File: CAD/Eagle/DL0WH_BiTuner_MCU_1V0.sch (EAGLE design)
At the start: 133 parts, among them Q0321 ABS07-32.768KHZ, U0101 STM32L476RXT_64PIN_LDO, U2401 LM53603-Q1, U8921 TS5A23166, U8951 OPA354, U9001 TPS62051, U9401 MC33996, U9501 MC33996, U9601 MC33996, U9801 MAX232_SOIC16, U9901 MAX232_SOIC16, X2411 WIRE-TO-BOARD_5MM08_1X02, X3201 MOLEX 105017-0001, X3301 SMA_SMT_AMPHENOL-901-143, X3311 SAMTEC SMA-J-P-H-RA-TH1, X9851 WIRE-TO-BOARD_5MM08_1X02, X9852 WIRE-TO-BOARD_5MM08_1X02, X9853 WIRE-TO-BOARD_5MM08_1X02, X9951 WIRE-TO-BOARD_5MM08_1X02, X9952 WIRE-TO-BOARD_5MM08_1X02, X9953 WIRE-TO-BOARD_5MM08_1X02

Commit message: HW_1V0 - CAD/Eagle - some routing done
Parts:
- L9011: device df4iah_rcl:L-EUL0603 -> df4iah_rcl:L-EU8.00X8.00MM
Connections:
- removed net +5V0: C2421.1, C2422.1, C2423.1, C9001.1, L2411.1, R2411.2, R9002.2, U2401.FB, U9001.EN, U9001.VIN
- removed net DC_12V_IN: C2401.1, C2402.1, C2403.1, C2404.1, U2401.EN, U2401.VIN@12, U2401.VIN@13, X2411.1
- net +12V: now also C2401.1, C2402.1, C2403.1, C2404.1, U2401.EN, U2401.VIN@12, U2401.VIN@13, X2411.1
- net +5V: now also C2421.1, C2422.1, C2423.1, C9001.1, L2411.1, R2411.2, R9002.2, U2401.FB, U9001.EN, U9001.VIN
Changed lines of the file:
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@@
 <part name="R9424" library="df4iah_rcl" deviceset="R-EU_" device="R0603" value="47R"/>
 <part name="U9001" library="df4iah_powersupply" deviceset="TPS62051" device=""/>
-<part name="L9011" library="df4iah_rcl" deviceset="L-EU" device="L0603" value="10uH"/>
+<part name="L9011" library="df4iah_rcl" deviceset="L-EU" device="8.00X8.00MM" value="10uH"/>
 <part name="R9021" library="df4iah_rcl" deviceset="R-EU_" device="R0603" value="1MR"/>
 <part name="R9022" library="df4iah_rcl" deviceset="R-EU_" device="R0603" value="1MR"/>
@@
 </busses>
 <nets>
-<net name="+5V0" class="0">
+<net name="+5V" class="2">
 <segment>
 <wire x1="182.88" y1="124.46" x2="195.58" y2="124.46" width="0.1524" layer="91"/>
@@
 </segment>
 </net>
-<net name="DC_12V_IN" class="0">
+<net name="+12V" class="0">
 <segment>
 <label x="22.86" y="124.46" size="1.778" layer="95" rot="R180" xref="yes"/>
@@
 </segment>
 </net>
-<net name="+5V0" class="0">
+<net name="+5V" class="2">
 <segment>
 <pinref part="U9001" gate="G$1" pin="VIN"/>

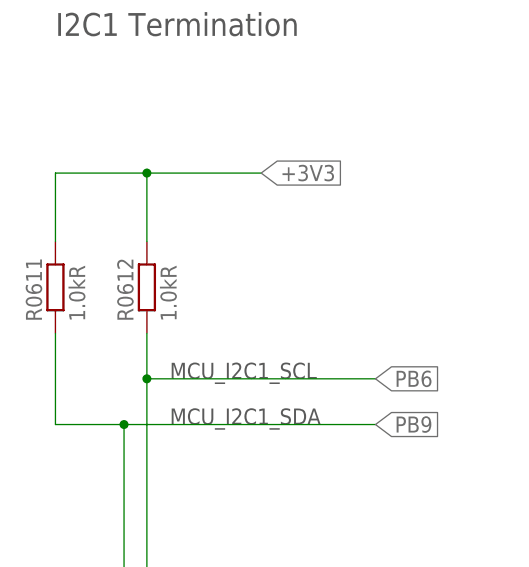
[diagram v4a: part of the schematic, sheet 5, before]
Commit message: HW_1V0 - CAD/Eagle - prepared BOM and adjusted some package sizes - still L9011 needs correct package
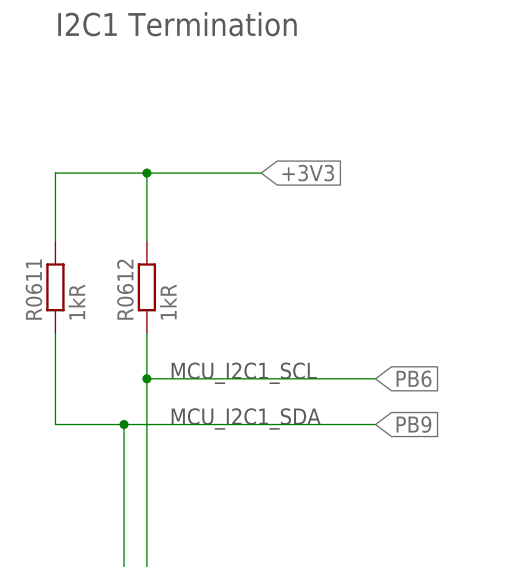
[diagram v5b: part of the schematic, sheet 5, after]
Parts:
- C0410, C2401, C2402, C2403, C2405, C2421, C2422, C2423: device df4iah_rcl:C-EUC0402 -> df4iah_rcl:C-EUC0603
- C8901, C8911, C8921, C8951, C9401, C9402, C9501, C9502, C9601, C9602: device df4iah_rcl:C-EUC0603 -> df4iah_rcl:C-EUC0402
- C9001, C9011: device df4iah_rcl:C-EUC0805 -> df4iah_rcl:C-EUC0603
- C9801, C9802, C9803, C9804, C9805, C9901, C9902, C9903, C9904, C9905: device rcl:C-EUC0805 -> df4iah_rcl:C-EUC0402
- L9011: device df4iah_rcl:L-EU8.00X8.00MM -> df4iah_rcl:L-EU4.90X4.90MM
- R0611, R0612: value 1.0kR -> 1kR
- R8901, R8902, R8903, R8911, R8912, R8913, R8921, R8922, R8951, R8952, R8961, R9001, R9002, R9021, R9022, R9411, R9424, R9511, R9524, R9611, R9621, R9622, R9623, R9624, R9625, R9626, R9801, R9802, R9803, R9804, R9901, R9902, R9903, R9904: device df4iah_rcl:R-EU_R0603 -> df4iah_rcl:R-EU_R0402
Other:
- note added: "Abracon ASPI-6045S-2R2N-T 6.0mm x 6.0mm"
- note added: "MURATA LQH43PN100M26L 4.5mm x 3.2mm"
- note added: "TODO !!!"
- note removed: "Abracon ASPI-6045S-2R2N-T 6.00mm x 6.00mm"
- note removed: "WE PD 744 777 10 8.00mm x 8.00mm"
